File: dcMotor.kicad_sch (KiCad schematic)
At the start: 121 parts, among them J1 USB_C_Receptacle_USB2.0_16P, J2 USB_C_Receptacle_USB2.0_16P, J3 Conn_ST_STDC14, J6 Conn_01x02_Pin, J7 Conn_01x04_Pin, J8 Conn_01x06_Pin, Q1 AO3400A, SW1 SW_Push, SW2 SW_Push, U1 LMR54406DBVR, U10 MCP6561-OT, U11 NUCLEO-L432KC, U2 NCP718ASNADJT1G, U3 NCP718ASNADJT1G, U5 TLV9152IDR, U6 ER_OLEDM0.91_1x-I2C, U7 STM32G431CBTx, U8 LTH-301-05, U9 DRV8231ADDA

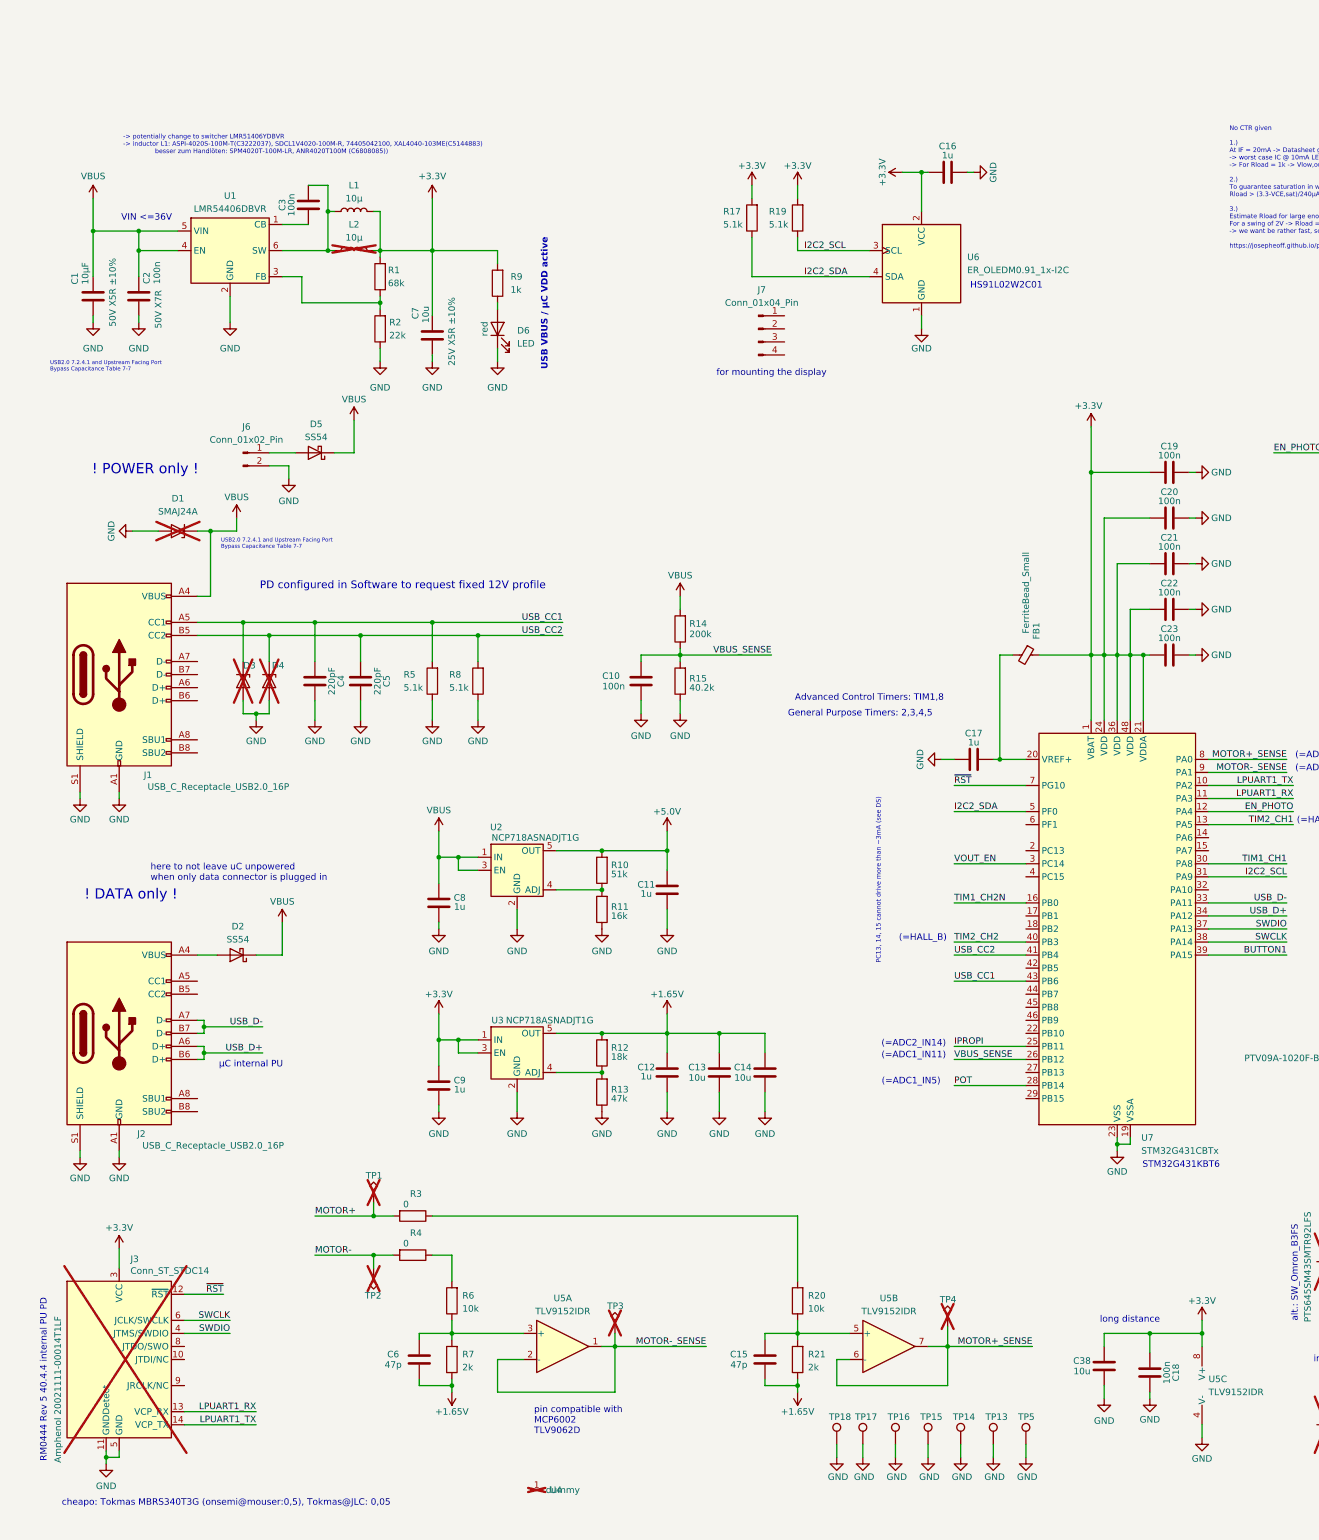
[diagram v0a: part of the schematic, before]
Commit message: remove more parts to reduce costs
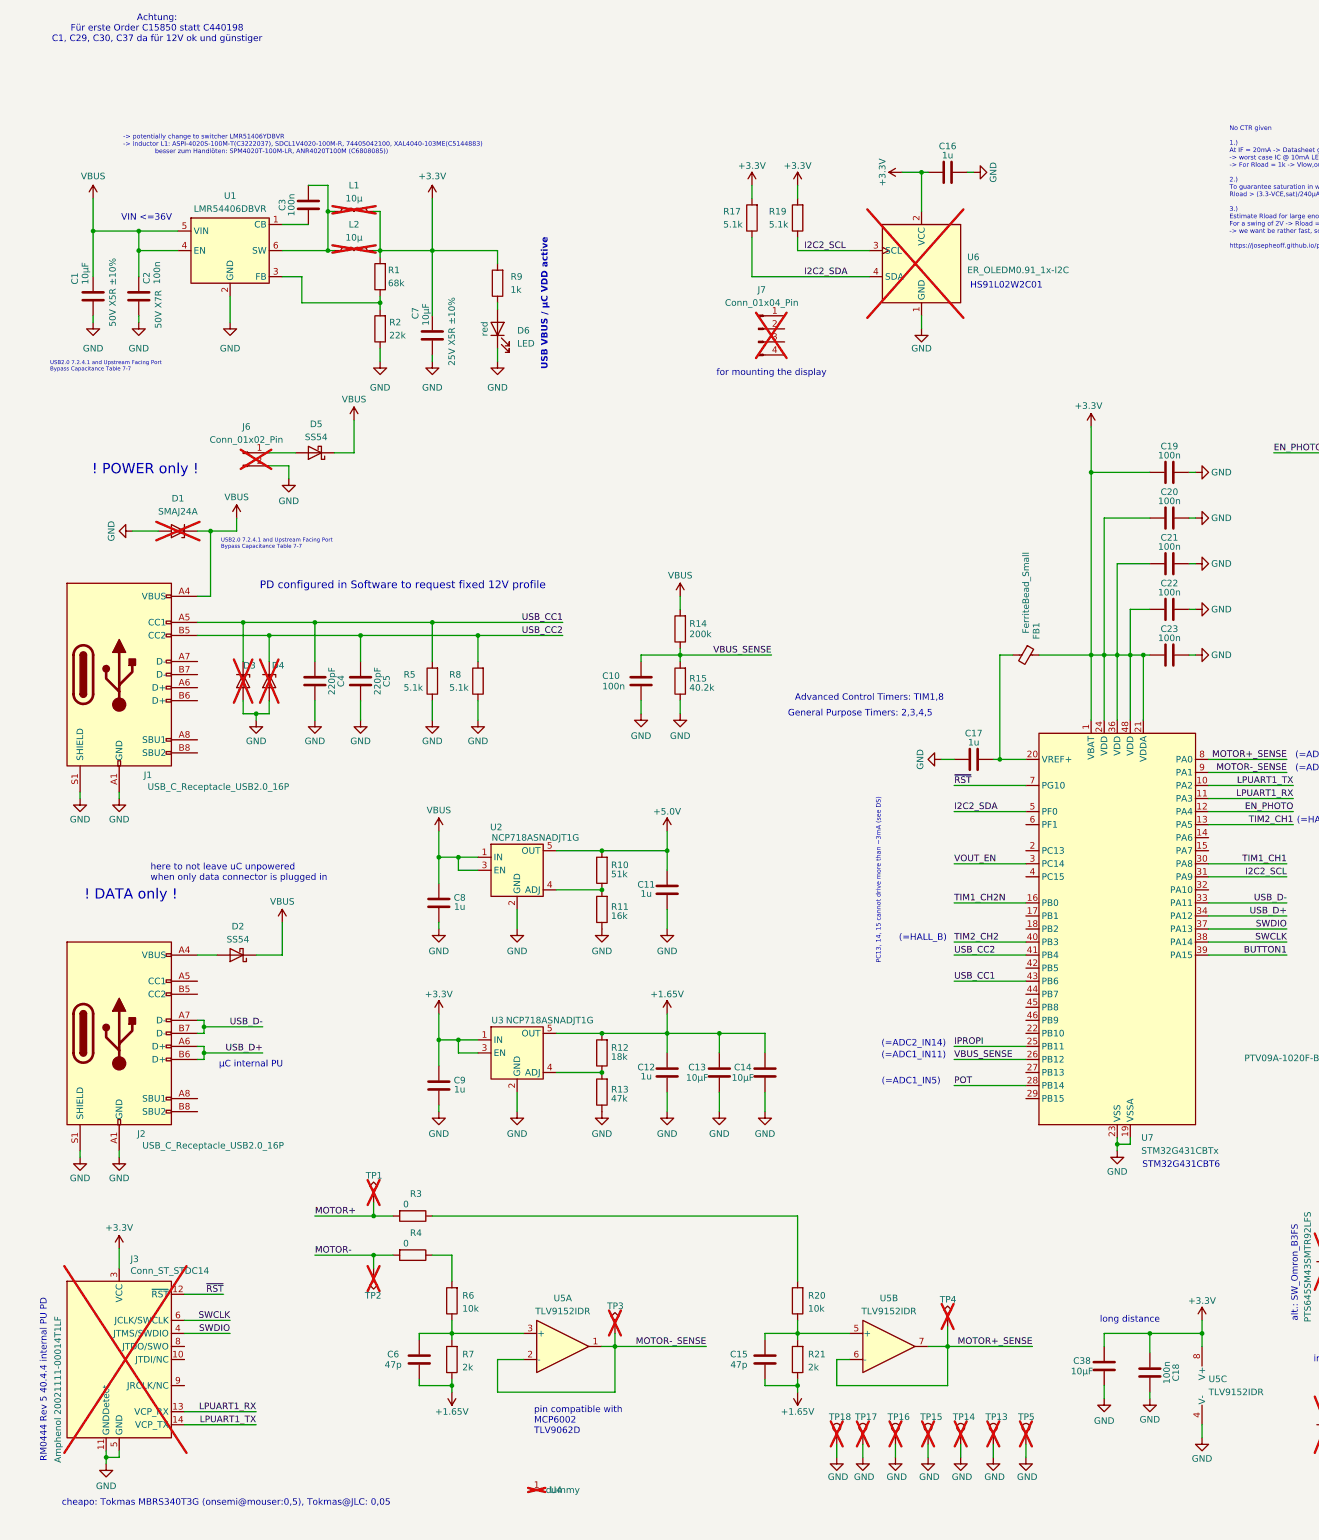
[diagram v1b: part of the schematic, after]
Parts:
- C1, C29, C30, C37: LCSC Part # C440198 -> C15850
- C13, C14, C38, C7: value 10u -> 10µF
- J6, L1, TP13, TP14, TP15, TP16, TP17, TP18, TP5, U6: now not fitted
- J7: FT Rotation Offset (none) -> 90; now not fitted
- U2, U3: FT Rotation Offset (none) -> 90
- U7: LCSC Part # C5270317 -> C529355
- U9: FT Rotation Offset (none) -> 270
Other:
- note added: "Achtung: Für erste Order C15850 statt C440198 C1, C29, C30, C37 da für 12V ok und günstiger"
- note added: "STM32G431CBT6"
- note removed: "STM32G431KBT6"
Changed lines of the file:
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@@
 		)
 	)
-	(text "STM32G431KBT6"
+	(text "STM32G431CBT6"
 		(exclude_from_sim no)
 		(at 237.236 217.424 0)
@@
 		)
 	)
+	(text "Achtung:\nFür erste Order C15850 statt C440198\nC1, C29, C30, C37 da für 12V ok und günstiger"
+		(exclude_from_sim no)
+		(at 37.846 -3.81 0)
+		(effects
+			(font
+				(size 1.27 1.27)
+			)
+		)
+	)
 	(text "USB VBUS / µC VDD active"
 		(exclude_from_sim no)
@@
 			)
 		)
-		(property "Value" "10u"
+		(property "Value" "10µF"
 			(at 143.002 200.406 0)
 			(show_name no)
@@
 		(on_board yes)
 		(in_pos_files yes)
-		(dnp no)
+		(dnp yes)
 		(fields_autoplaced yes)
 		(property "Reference" "J6"
@@
 		(on_board yes)
 		(in_pos_files yes)
-		(dnp no)
+		(dnp yes)
 		(property "Reference" "L1"
 			(at 76.2 26.67 90)
@@
 			)
 		)
-		(property "Value" "10u"
+		(property "Value" "10µF"
 			(at 217.932 257.556 0)
 			(show_name no)
@@
 			)
 		)
+		(property "FT Rotation Offset" "90"
+			(at 107.95 195.58 0)
+			(hide yes)
+			(show_name no)
+			(do_not_autoplace no)
+			(effects
+				(font
+					(size 1.27 1.27)
+				)
+			)
+		)
 		(pin "4"
 		)
@@
 			)
 		)
-		(property "LCSC Part #" "C440198"
+		(property "LCSC Part #" "C15850"
 			(at 341.63 113.03 0)
 			(hide yes)
@@
 			)
 		)
-		(property "LCSC Part #" "C5270317"
+		(property "LCSC Part #" "C529355"
+			(at 224.79 171.45 0)
+			(hide yes)
+			(show_name no)
+			(do_not_autoplace no)
+			(effects
+				(font
+					(size 1.27 1.27)
+				)
+			)
+		)
+		(property "FT Rotation Offset" ""
 			(at 224.79 171.45 0)
 			(hide yes)
@@
 			)
 		)
-		(property "LCSC Part #" "C440198"
+		(property "LCSC Part #" "C15850"
 			(at 341.63 120.65 0)
 			(hide yes)
@@
 		(on_board yes)
 		(in_pos_files yes)
-		(dnp no)
+		(dnp yes)
 		(property "Reference" "TP5"
 			(at 205.486 266.446 0)
@@
 		(on_board yes)
 		(in_pos_files yes)
-		(dnp no)
+		(dnp yes)
 		(fields_autoplaced yes)
 		(property "Reference" "J7"
@@
 			)
 		)
+		(property "FT Rotation Offset" "90"
+			(at 154.94 54.61 0)
+			(hide yes)
+			(show_name no)
+			(do_not_autoplace no)
+			(effects
+				(font
+					(size 1.27 1.27)
+				)
+			)
+		)
 		(pin "3"
 		)
@@
 			)
 		)
-		(property "Value" "10u"
+		(property "Value" "10µF"
 			(at 90.17 51.816 90)
 			(show_name no)
@@
 		(on_board yes)
 		(in_pos_files yes)
-		(dnp no)
+		(dnp yes)
 		(property "Reference" "TP13"
 			(at 199.136 266.446 0)
@@
 			)
 		)
-		(property "Value" "10u"
+		(property "Value" "10µF"
 			(at 151.892 200.406 0)
 			(show_name no)
@@
 			)
 		)
-		(property "LCSC Part #" "C440198"
+		(property "LCSC Part #" "C15850"
 			(at 25.4 48.26 0)
 			(hide yes)
@@
 		(on_board yes)
 		(in_pos_files yes)
-		(dnp no)
+		(dnp yes)
 		(property "Reference" "TP18"
 			(at 168.656 266.446 0)
@@
 		(on_board yes)
 		(in_pos_files yes)
-		(dnp no)
+		(dnp yes)
 		(property "Reference" "TP17"
 			(at 173.736 266.446 0)
@@
 			)
 		)
+		(property "FT Rotation Offset" "90"
+			(at 107.95 160.02 0)
+			(hide yes)
+			(show_name no)
+			(do_not_autoplace no)
+			(effects
+				(font
+					(size 1.27 1.27)
+				)
+			)
+		)
 		(pin "4"
 		)
@@
 		(on_board yes)
 		(in_pos_files yes)
-		(dnp no)
+		(dnp yes)
 		(property "Reference" "TP16"
 			(at 180.086 266.446 0)
@@
 			)
 		)
-		(property "LCSC Part #" "C440198"
+		(property "LCSC Part #" "C15850"
 			(at 341.63 128.27 0)
 			(hide yes)
@@
 		(on_board yes)
 		(in_pos_files yes)
-		(dnp no)
+		(dnp yes)
 		(property "Reference" "TP14"
 			(at 192.786 266.446 0)
@@
 		(on_board yes)
 		(in_pos_files yes)
-		(dnp no)
+		(dnp yes)
 		(property "Reference" "TP15"
 			(at 186.436 266.446 0)
@@
 			)
 		)
+		(property "FT Rotation Offset" "270"
+			(at 355.6 152.4 0)
+			(hide yes)
+			(show_name no)
+			(do_not_autoplace no)
+			(effects
+				(font
+					(size 1.27 1.27)
+				)
+			)
+		)
 		(pin "8"
 		)
@@
 		(on_board yes)
 		(in_pos_files yes)
-		(dnp no)
+		(dnp yes)
 		(fields_autoplaced yes)
 		(property "Reference" "U6"
@@
 		)
 	)
-	(group "NCP718ASN-ADJ-3V3"
-		(lib_id "dcdc_lin:NCP718ASN-ADJ-3V3")
-		(members "087cab51-ca10-4d81-9758-96e601bc3384" "1164ab4b-7715-49d9-ae02-1223cf65ff4b"
-			"2ac937b7-5faf-40b6-9707-48dc70a7acf4" "39f0dc94-edff-4035-95b8-2651f78fdd9a"
-			"432e86de-6a64-4897-8756-467f61a6512a" "4b3e3a9d-2303-491a-a5f6-43ba34f1a43f"
-			"58aaacc0-f006-4dd4-b569-22a8ea36df80" "642c1acf-fb78-4ecf-b52a-7530b7583f61"
-			"6d1e340a-d8a1-400d-b242-401b39055000" "71d3b8a3-7d0d-4514-9651-c00f2b4c1909"
-			"7c1c4822-8859-46be-a3cd-432d718b0505" "810997df-c2c9-4a98-927c-c7fc92ece93b"
-			"82954d61-2ba6-4fd3-aa79-f41d8e461c90" "855a23d4-7eee-49b3-bdf4-97c0906ed207"
-			"878c5705-08ca-4ccb-8eb9-f544bb3af368" "881c09ee-a59b-4d93-92c1-dc5279f9037b"
-			"8ccb6454-afc3-40b0-a10c-2700b75c35bf" "8e5dbe06-0697-4440-a67f-c32720d714f3"
-			"9d1a297c-aa52-4ff7-bb10-a343c5602381" "9f87b0b0-f26b-44dd-8fda-52403b755fb7"
-			"a2f10698-ffde-46c8-8519-f806c3dd4742" "ad9818c5-c432-47a2-b533-b0b8ffde5d3d"
-			"c860acc2-2ea1-4b2e-b93c-ce5e83cd536b" "d1dbb36c-dd21-44fb-8f9c-055090f6d1a6"
-			"d992b2fa-e0c7-4d16-b386-097116bffc40" "da0cdd17-b532-4430-b357-ed677d57b24c"
-			"eb88c730-9920-49b7-bceb-fca374e81791" "f2b9d823-ba28-4ee1-a715-c583537fdc2d"
-			"f9592511-83c0-4003-ba96-6caf06ddf103" "fc5cb574-912f-429f-acac-2c80450f96bc"
-		)
-	)
-	(group "DCDC_LMR544060"
-		(lib_id "dcdc_sw:DCDC_LMR544060")
-		(members "045d2508-22d9-45c4-8287-9260665b9ad0" "058a1874-5b25-4672-b67a-8fa7ff0563d2"
-			"082983a2-ef38-4909-87fc-02ab1561380f" "0aaa86ac-67cc-4d9a-b556-7dc4e62a3ce4"
-			"0c5a651f-2d78-467f-8d83-f9f006aede95" "0ef8cf4d-2f69-4ffb-b6ac-10be32d2a991"
-			"1790d66f-3553-4ccb-aeea-01437161b75e" "1ca4125a-3d1b-4c6c-a07f-d8c1deed7377"
-			"1f4fec2f-f5d7-45b1-a188-83ab5a58c207" "2132680a-e572-4bd7-bf52-7a60a3209c56"
-			"21dcae7b-1541-4bc6-a7e2-09cc6c241637" "22e343b2-6464-45af-b003-09e184497e76"
-			"23a58a11-21e8-442d-884c-bf9425e18e93" "24e73d74-7856-4747-ad76-fcc01c29022b"
-			"25914bde-24df-42b4-bdf4-633096424b94" "3193d417-afdb-4512-b04b-c8238ef1f9c5"
-			"3590cf87-d5e4-46e0-b9d3-e4c71b8a0e74" "35d8c716-451f-4e35-8f53-880892479593"
-			"36e8f6f7-ab3f-456f-8e72-7bae36c274fa" "370d5437-1f13-4f86-b3c3-4ccf83c33b27"
-			"3938f4bb-bc2f-4402-90e9-225717053e83" "4400241c-3006-4d1f-b147-405a29d2ea44"
-			"491e4011-f2b2-43c3-a786-e1333a0b1e78" "4cf08774-4ad6-4ac1-9821-52c421ca36ea"
-			"4d347f68-68fa-4d69-8d49-279da4478d0a" "504084f7-fb61-4c63-b16e-ab1804fd9d23"
-			"5b021a70-997a-4b2d-b91a-31b7a2ed61c9" "5deaf6cc-7db1-4ebc-adda-e4fd5757f132"
-			"63501c5e-b413-44bf-84cb-75a8775b7e03" "6a0ffa03-5718-4c31-b18a-8a4e22305355"
-			"6bd379f3-0e4e-4de4-84f8-9817fd1472b7" "6d6aa3a8-927d-4f63-9791-c6cef9eb925b"
-			"6f10fab1-4215-4fe9-af83-f3f188077c5d" "6fd988fa-ab16-47de-851d-f7c5d8c8c157"
-			"70d57abe-896a-4b3f-be97-10ce9f40c8fd" "78c69c17-56f5-49f4-b08c-683a79536c2f"
-			"825a3daa-6051-4893-b21c-64958955d4fb" "8348bb1c-9bb0-436e-aa1e-74c9b7f86fd1"
-			"83c6cdb6-3bf8-4e3b-a5ac-c2626a53abdf" "874bff08-58f1-4e98-b69a-fa4282722259"
-			"88c60945-d3c1-48e2-be99-731e394db7df" "8b787a2c-53e1-4aae-a3ba-b74da894bcd9"
-			"8ce37b43-32e3-4d84-afc9-85792cec1921" "9176afe6-e3c7-4b7c-a3e9-1d487b623059"
-			"954438f4-4076-440b-b741-d2aa99df7ae3" "96d5909b-671e-44e7-be27-a13428c33225"
-			"976fc8fb-82e3-427b-8c68-1dd90c026cd2" "987cce70-eeaa-49d7-b446-c969f8fcc364"
-			"9eeace40-1f7b-4c73-b1cb-72297b76992b" "a3600cb7-5a44-48e0-8723-ec1a337516ec"
-			"a9625c8f-2b03-4686-bc4c-b2b57e1e57a2" "a9c329c4-7076-4173-968e-584a9b5c3355"
-			"aca66297-985f-4af0-b9c3-a540406a5d1e" "aedf631f-d55a-4835-a632-cd47a87eb44b"
-			"c22ca3ac-9223-45e7-9a48-4930aebfbda7" "c6d3b4c0-1588-4cb3-9ad4-c32fbb3fdda3"
-			"ca1b7c5c-452c-4a46-b5e7-4579ccf37fc0" "ca9a01f6-2891-4d8c-aa24-3e96bcc83660"
-			"ce22da76-c260-4d1a-990f-6b714b75c203" "cf1b7ec3-de97-45be-b640-b2132a7442b0"
-			"d74f2649-5034-4892-be25-50edc1396cdf" "f0284f1f-8e9e-4f7f-b3a8-3a1c86dffd9b"
-			"f4e7a83c-f265-4be4-b4b1-9bfbefa25ae8" "f84c5de0-75ac-47b9-9d01-1704064d283c"
-			"fa0fd0e0-c1f2-4bd0-b608-142373744cfc" "fb65f4ed-f78e-49b2-bcf1-0492be0fc792"
-		)
-	)
